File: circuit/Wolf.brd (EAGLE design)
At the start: 100 x 56 mm, 21 parts, among them IC1 74LS595N, K1 SNES, M1 ARDUINO-NANO-3.0

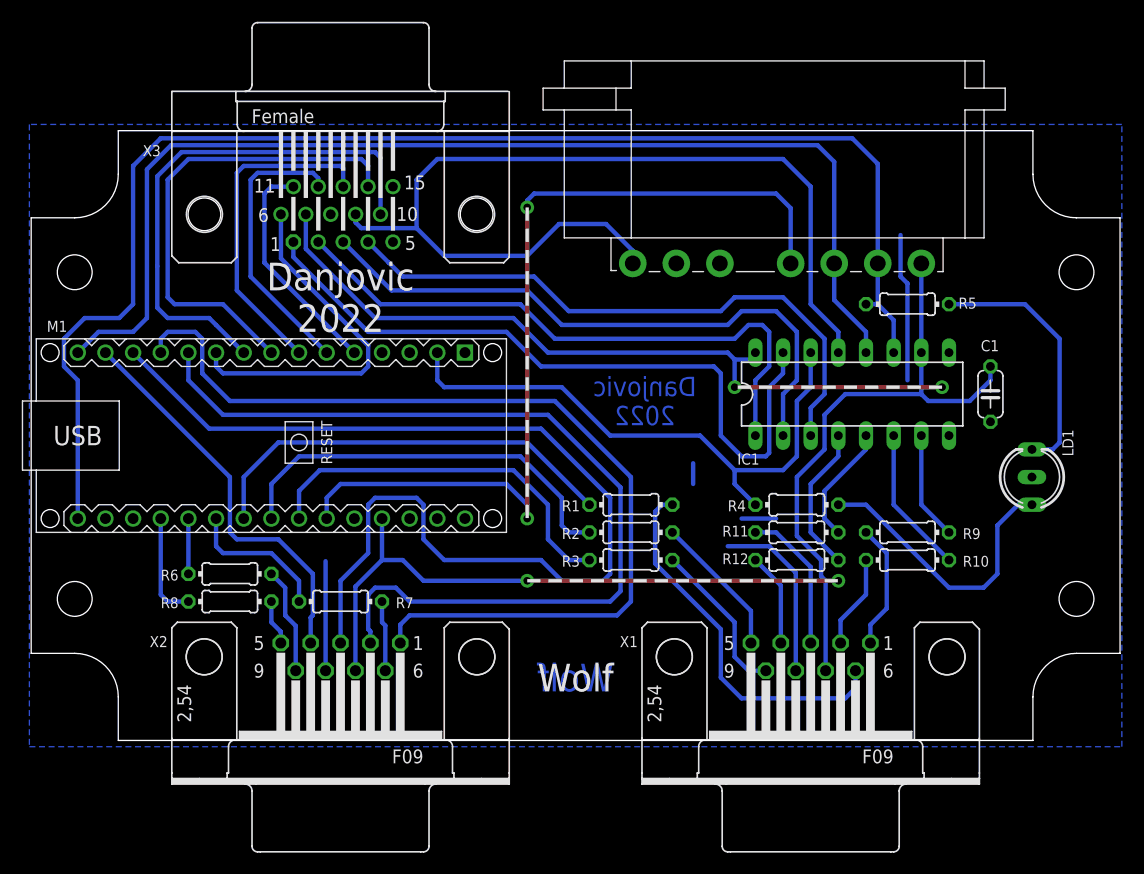
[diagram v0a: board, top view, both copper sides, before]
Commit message: Added missing connection to GND
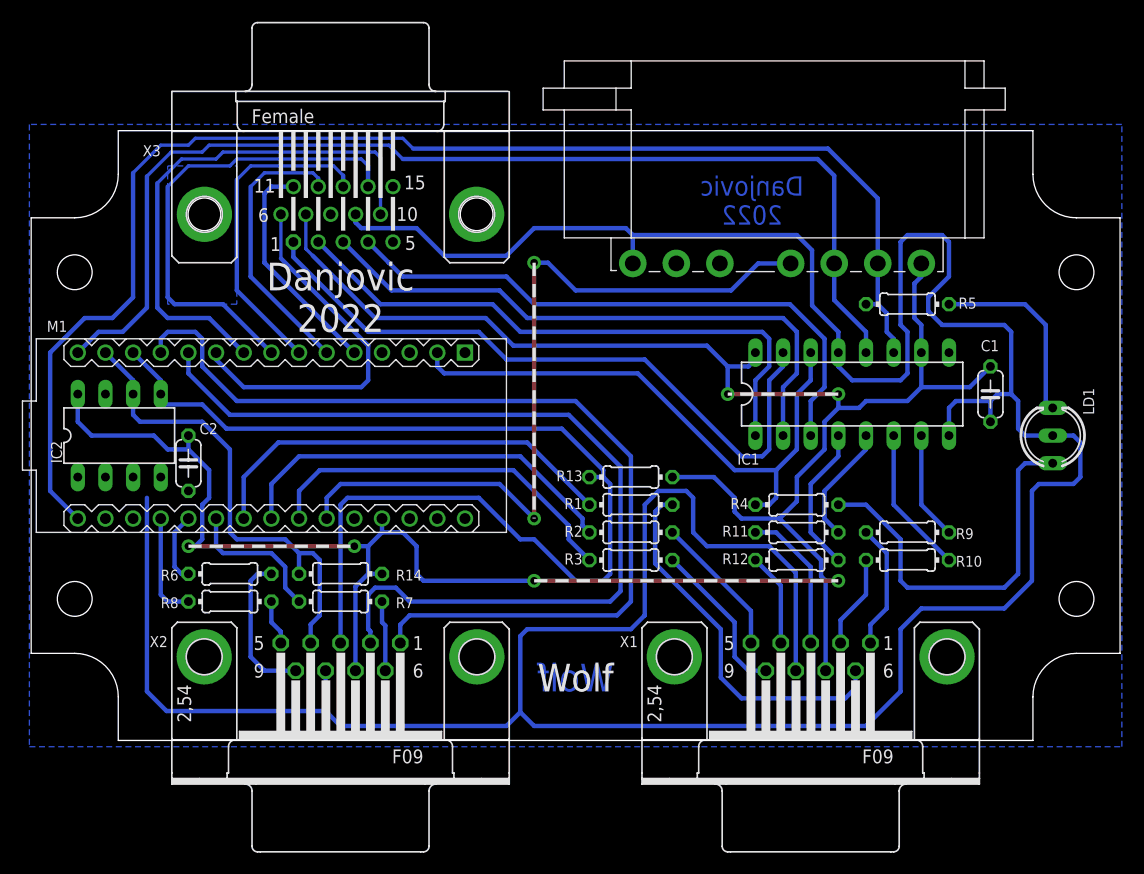
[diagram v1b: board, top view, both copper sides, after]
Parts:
- added C2: 100n, rcl:C050-024X044
- added IC2: 24LC256P, microchip:DIL8
- added R13, R14: 10k, rcl:0204/7
- X1, X2: device con-subd:F09H -> con-subd:F09HP
- moved LD1 4.26 mm to (94.6, 27.9)
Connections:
- removed net GND.1: M1.J1.4
- removed net ROW3: M1.J1.13, X2.3
- removed net ROW4: M1.J1.14, X2.4
- new net ROW3/SDA: IC2.5, M1.J1.13, R13.1, X2.3
- new net ROW4/SCL: IC2.6, M1.J1.14, R14.1, X2.4
- net +5V: now also C2.1, IC2.8, R13.2, R14.2
- net GND: now also C2.2, IC2.1, IC2.2, IC2.3, IC2.4, IC2.7, M1.J1.4
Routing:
- net GND: track 134.6 -> 314.3 mm
- net ROW3/SDA: track 0.00 -> 101.0 mm
- net ROW3: track 97.8 -> 0.00 mm
- net +5V: track 187.6 -> 236.5 mm, vias 4 -> 6
- net ROW4/SCL: track 0.00 -> 43.8 mm
- net ROW4: track 36.9 -> 0.00 mm
- net DIN: track 82.2 -> 71.9 mm
- net N$1: track 26.7 -> 35.4 mm
- net N$2: track 23.8 -> 17.6 mm
- net R_COL2: track 9.82 -> 13.8 mm
- net J3/J4: track 65.9 -> 62.3 mm
- net LATCH: track 104.7 -> 103.1 mm
- net CLOCK: track 126.8 -> 125.3 mm
- net J2/J5: track 55.9 -> 54.5 mm
- net B0/LP: track 33.1 -> 34.5 mm
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- added copper zone on layer 16, net N$3
